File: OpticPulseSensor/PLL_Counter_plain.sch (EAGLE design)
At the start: 14 parts, among them IC1 NE567N, IC2 CNY70, T1 BC547

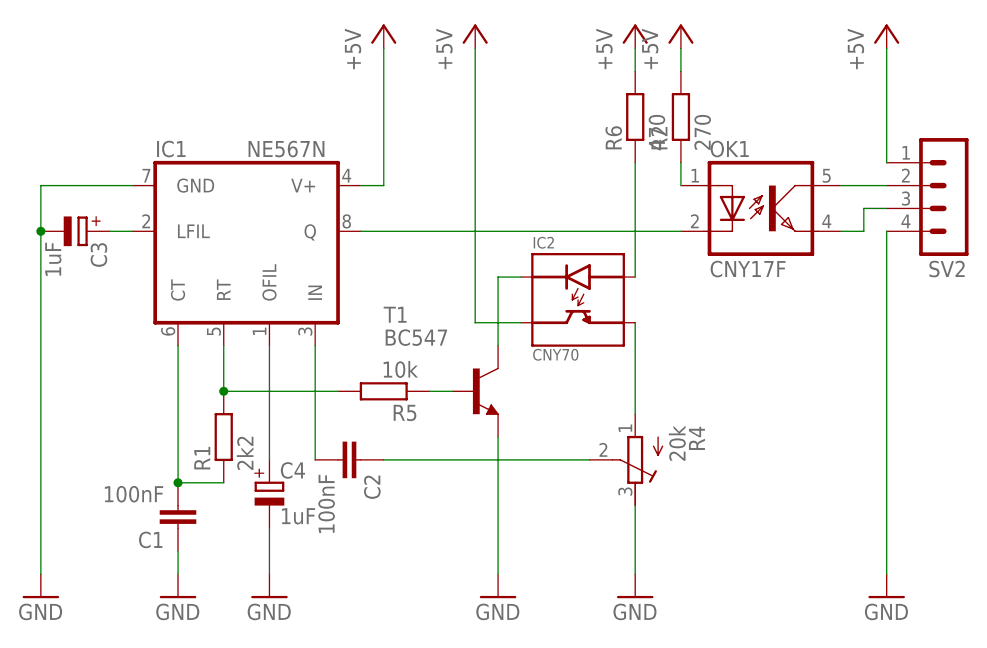
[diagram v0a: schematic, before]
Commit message: Optoreader with accuracy trimming
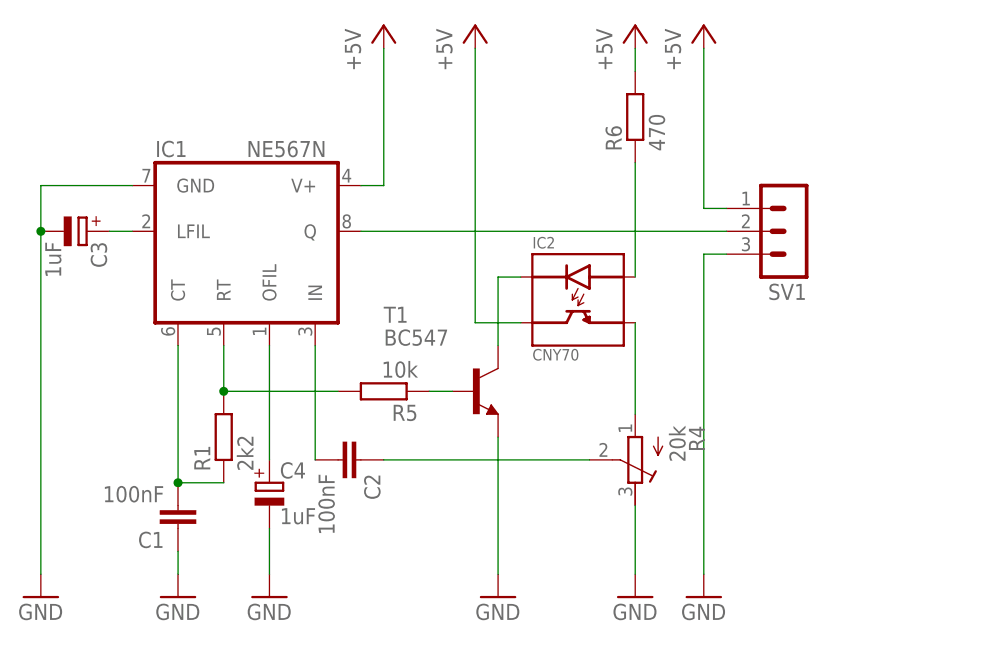
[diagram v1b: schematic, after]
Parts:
- removed OK1: CNY17F, optocoupler:CNY17F
- removed R2: 270, resistor:R-EU_0204/7
- removed SV2: (no value), con-lstb:MA04-1
- added SV1: (no value), con-lstb:MA03-1
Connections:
- removed net N$13: OK1.EMIT, SV2.3
- removed net N$5: OK1.A, R2.1
- removed net N$9: OK1.COL, SV2.2
- net +5V: now also SV1.1; no longer R2.2, SV2.1
- net GND: now also SV1.3; no longer SV2.4
- net N$4: now also SV1.2; no longer OK1.C
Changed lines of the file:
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@@
 <part name="C4" library="resistor" deviceset="CPOL-EU" device="E2.5-5" value="1uF"/>
 <part name="GND5" library="supply1" deviceset="GND" device=""/>
-<part name="P+4" library="supply1" deviceset="+5V" device=""/>
 <part name="GND6" library="supply1" deviceset="GND" device=""/>
 <part name="P+5" library="supply1" deviceset="+5V" device=""/>
-<part name="OK1" library="optocoupler" deviceset="CNY17F" device=""/>
-<part name="SV2" library="con-lstb" deviceset="MA04-1" device=""/>
-<part name="R2" library="resistor" deviceset="R-EU_" device="0204/7" value="270"/>
 <part name="P+2" library="supply1" deviceset="+5V" device=""/>
 <part name="R4" library="rcl" deviceset="R-TRIMM" device="64X" value="20k"/>
+<part name="SV1" library="con-lstb" deviceset="MA03-1" device=""/>
 </parts>
 <sheets>
@@
 <instance part="C4" gate="G$1" x="58.42" y="40.64"/>
 <instance part="GND5" gate="1" x="58.42" y="27.94"/>
-<instance part="P+4" gate="1" x="104.14" y="91.44"/>
-<instance part="GND6" gate="1" x="127" y="27.94"/>
+<instance part="GND6" gate="1" x="106.68" y="27.94"/>
 <instance part="P+5" gate="1" x="81.28" y="91.44"/>
-<instance part="OK1" gate="G$1" x="114.3" y="71.12"/>
-<instance part="SV2" gate="1" x="134.62" y="71.12" rot="R180"/>
-<instance part="R2" gate="G$1" x="104.14" y="81.28" rot="R90"/>
-<instance part="P+2" gate="1" x="127" y="91.44"/>
+<instance part="P+2" gate="1" x="106.68" y="91.44"/>
 <instance part="R4" gate="G$1" x="99.06" y="43.18" rot="R180"/>
+<instance part="SV1" gate="G$1" x="116.84" y="68.58" rot="R180"/>
 </instances>
 <busses>
@@
 </segment>
 <segment>
-<pinref part="SV2" gate="1" pin="4"/>
-<pinref part="GND6" gate="1" pin="GND"/>
-<wire x1="127" y1="68.58" x2="127" y2="30.48" width="0.1524" layer="91"/>
-</segment>
-<segment>
 <pinref part="R4" gate="G$1" pin="E"/>
 <pinref part="GND3" gate="1" pin="GND"/>
 <wire x1="99.06" y1="38.1" x2="99.06" y2="30.48" width="0.1524" layer="91"/>
+</segment>
+<segment>
+<pinref part="SV1" gate="G$1" pin="3"/>
+<pinref part="GND6" gate="1" pin="GND"/>
+<wire x1="109.22" y1="66.04" x2="106.68" y2="66.04" width="0.1524" layer="91"/>
+<wire x1="106.68" y1="66.04" x2="106.68" y2="30.48" width="0.1524" layer="91"/>
 </segment>
 </net>
@@
 </segment>
 <segment>
-<pinref part="P+4" gate="1" pin="+5V"/>
-<pinref part="R2" gate="G$1" pin="2"/>
-<wire x1="104.14" y1="88.9" x2="104.14" y2="86.36" width="0.1524" layer="91"/>
-</segment>
-<segment>
 <pinref part="P+2" gate="1" pin="+5V"/>
-<pinref part="SV2" gate="1" pin="1"/>
-<wire x1="127" y1="88.9" x2="127" y2="76.2" width="0.1524" layer="91"/>
+<wire x1="106.68" y1="88.9" x2="106.68" y2="71.12" width="0.1524" layer="91"/>
+<pinref part="SV1" gate="G$1" pin="1"/>
+<wire x1="106.68" y1="71.12" x2="109.22" y2="71.12" width="0.1524" layer="91"/>
 </segment>
 </net>
@@
 </segment>
 </net>
-<net name="N$4" class="0">
-<segment>
-<pinref part="IC1" gate="A" pin="Q"/>
-<pinref part="OK1" gate="G$1" pin="C"/>
-<wire x1="68.58" y1="68.58" x2="104.14" y2="68.58" width="0.1524" layer="91"/>
-</segment>
-</net>
-<net name="N$5" class="0">
-<segment>
-<pinref part="R2" gate="G$1" pin="1"/>
-<pinref part="OK1" gate="G$1" pin="A"/>
-<wire x1="104.14" y1="76.2" x2="104.14" y2="73.66" width="0.1524" layer="91"/>
-</segment>
-</net>
-<net name="N$9" class="0">
-<segment>
-<pinref part="OK1" gate="G$1" pin="COL"/>
-<pinref part="SV2" gate="1" pin="2"/>
-<wire x1="121.92" y1="73.66" x2="127" y2="73.66" width="0.1524" layer="91"/>
-</segment>
-</net>
-<net name="N$13" class="0">
-<segment>
-<pinref part="OK1" gate="G$1" pin="EMIT"/>
-<wire x1="121.92" y1="68.58" x2="124.46" y2="68.58" width="0.1524" layer="91"/>
-<wire x1="124.46" y1="68.58" x2="124.46" y2="71.12" width="0.1524" layer="91"/>
-<pinref part="SV2" gate="1" pin="3"/>
-<wire x1="124.46" y1="71.12" x2="127" y2="71.12" width="0.1524" layer="91"/>
-</segment>
-</net>
 <net name="N$7" class="0">
 <segment>
@@
 </segment>
 </net>
+<net name="N$4" class="0">
+<segment>
+<pinref part="IC1" gate="A" pin="Q"/>
+<pinref part="SV1" gate="G$1" pin="2"/>
+<wire x1="68.58" y1="68.58" x2="109.22" y2="68.58" width="0.1524" layer="91"/>
+</segment>
+</net>
